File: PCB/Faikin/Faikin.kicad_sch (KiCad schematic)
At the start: 28 parts, among them J1 1x5, J2 TC2030-USB-NL-DS, J3 Reset, Q1 BSS138PS, U2 ESP32-S3-MINI-1, U3 MD8942

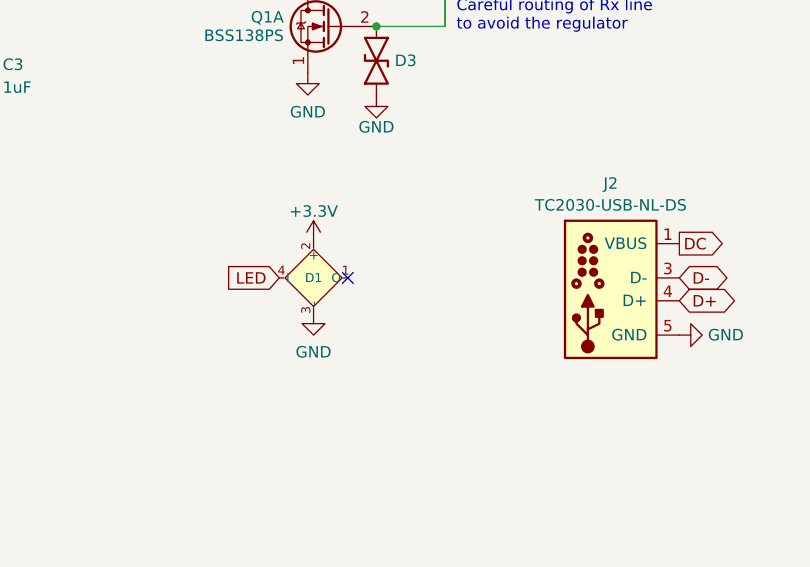
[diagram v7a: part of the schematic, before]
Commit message: Slight tweak for LED visibility from other side
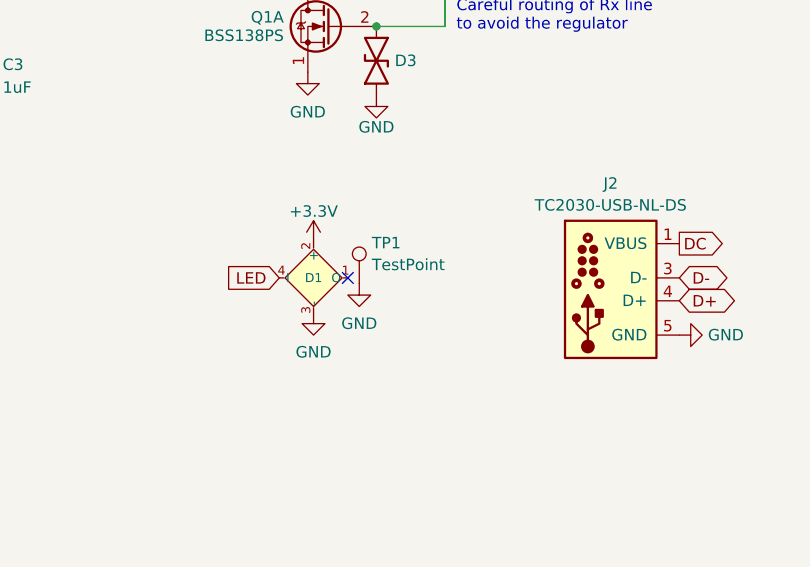
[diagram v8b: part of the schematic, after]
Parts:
- added TP1: TestPoint, RevK:1x2-Hole, symbol Connector:TestPoint
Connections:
- net GND: now also TP1.1
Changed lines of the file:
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@@
+	)
+	(symbol
+		(lib_id "Connector:TestPoint")
+		(at 165.1 136.525 0)
+		(unit 1)
+		(exclude_from_sim no)
+		(in_bom yes)
+		(on_board yes)
+		(dnp no)
+		(fields_autoplaced yes)
+		(property "Reference" "TP1"
+			(at 166.497 132.0108 0)
+			(effects
+				(font
+					(size 1.27 1.27)
+				)
+				(justify left)
+			)
+		)
+		(property "Value" "TestPoint"
+			(at 166.497 134.4351 0)
+			(effects
+				(font
+					(size 1.27 1.27)
+				)
+				(justify left)
+			)
+		)
+		(property "Footprint" "RevK:1x2-Hole"
+			(at 170.18 136.525 0)
+			(effects
+				(font
+					(size 1.27 1.27)
+				)
+				(hide yes)
+			)
+		)
+		(property "Datasheet" "~"
+			(at 170.18 136.525 0)
+			(effects
+				(font
+					(size 1.27 1.27)
+				)
+				(hide yes)
+			)
+		)
+		(property "Description" "test point"
+			(at 165.1 136.525 0)
+			(effects
+				(font
+					(size 1.27 1.27)
+				)
+				(hide yes)
+			)
+		)
+		(pin "1"
+		)
+		(instances
+			(project ""
+				(path "/46c350bb-7de4-4e81-aafd-4af55e37aab0"
+					(reference "TP1")
+					(unit 1)
+				)
+			)
+		)
 	)
 	(symbol
@@
 					(unit 1)
 				)
+			)
+		)
+	)
+	(symbol
+		(lib_id "power:GND")
+		(at 165.1 136.525 0)
+		(unit 1)
+		(exclude_from_sim no)
+		(in_bom yes)
+		(on_board yes)
+		(dnp no)
+		(fields_autoplaced yes)
+		(property "Reference" "#PWR027"
+			(at 165.1 142.875 0)
+			(effects
+				(font
+					(size 1.27 1.27)
+				)
+				(hide yes)
+			)
+		)
+		(property "Value" "GND"
+			(at 165.1 140.9684 0)
+			(effects
+				(font
+					(size 1.27 1.27)
+				)
+			)
+		)
+		(property "Footprint" ""
+			(at 165.1 136.525 0)
+			(effects
+				(font
+					(size 1.27 1.27)
+				)
+				(hide yes)
+			)
+		)
+		(property "Datasheet" ""
+			(at 165.1 136.525 0)
+			(effects
+				(font
+					(size 1.27 1.27)
+				)
+				(hide yes)
+			)
+		)
+		(property "Description" "Power symbol creates a global label with name \"GND\" , ground"
+			(at 165.1 136.525 0)
+			(effects
+				(font
+					(size 1.27 1.27)
+				)
+				(hide yes)
+			)
+		)
+		(pin "1"
+		)
+		(instances
+			(project "Faikin"
+				(path "/46c350bb-7de4-4e81-aafd-4af55e37aab0"
+					(reference "#PWR027")
+					(unit 1)
+				)
